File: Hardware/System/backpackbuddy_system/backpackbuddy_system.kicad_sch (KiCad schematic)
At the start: 20 parts, among them J1 PIR, J2 Ultrasonic 2, J3 Ultrasonic 1, J4 Left Vibration 1, J5 Left Vibration 2, J6 Raspberry Pi, J7 ESP8266, J8 Right Vibration 1, J9 Right Vibration 2, Q1 Q_NMOS_GSD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

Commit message: random other sch changes
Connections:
- net ESP RESET: now reaches J7.6 (Pin_6), SW1.1
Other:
- moved on the sheet: SW1
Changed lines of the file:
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@@
   (junction (at 181.61 153.67) (diameter 0) (color 0 0 0 0)
   )
-  (junction (at 217.17 63.5) (diameter 0) (color 0 0 0 0)
-  )
   (junction (at 222.25 135.89) (diameter 0) (color 0 0 0 0)
   )
@@
     (stroke (width 0) (type default) (color 0 0 0 0))
   )
+  (wire (pts (xy 232.41 62.23) (xy 243.84 62.23))
+    (stroke (width 0) (type default) (color 0 0 0 0))
+  )
   (wire (pts (xy 194.31 86.36) (xy 189.23 86.36))
     (stroke (width 0) (type default) (color 0 0 0 0))
@@
     (stroke (width 0) (type default) (color 0 0 0 0))
   )
-  (wire (pts (xy 212.09 63.5) (xy 217.17 63.5))
-    (stroke (width 0) (type default) (color 0 0 0 0))
-  )
   (wire (pts (xy 132.08 60.96) (xy 55.88 60.96))
     (stroke (width 0) (type default) (color 0 0 0 0))
@@
     (stroke (width 0) (type default) (color 0 0 0 0))
   )
-  (wire (pts (xy 217.17 38.1) (xy 217.17 63.5))
+  (wire (pts (xy 217.17 38.1) (xy 217.17 67.31))
     (stroke (width 0) (type default) (color 0 0 0 0))
   )
@@
     (stroke (width 0) (type default) (color 0 0 0 0))
   )
-  (wire (pts (xy 217.17 67.31) (xy 217.17 63.5))
-    (stroke (width 0) (type default) (color 0 0 0 0))
-  )
   (wire (pts (xy 119.38 96.52) (xy 118.11 96.52))
     (stroke (width 0) (type default) (color 0 0 0 0))
@@
     (stroke (width 0) (type default) (color 0 0 0 0))
   )
+  (wire (pts (xy 256.54 62.23) (xy 256.54 68.58))
+    (stroke (width 0) (type default) (color 0 0 0 0))
+  )
   (wire (pts (xy 102.87 118.11) (xy 132.08 118.11))
     (stroke (width 0) (type default) (color 0 0 0 0))
@@
     (stroke (width 0) (type default) (color 0 0 0 0))
   )
+  (wire (pts (xy 254 62.23) (xy 256.54 62.23))
+    (stroke (width 0) (type default) (color 0 0 0 0))
+  )
   (wire (pts (xy 163.83 120.65) (xy 163.83 123.19))
     (stroke (width 0) (type default) (color 0 0 0 0))
@@
     (stroke (width 0) (type default) (color 0 0 0 0))
   )
-  (wire (pts (xy 201.93 50.8) (xy 201.93 63.5))
-    (stroke (width 0) (type default) (color 0 0 0 0))
-  )
   (wire (pts (xy 222.25 153.67) (xy 226.06 153.67))
     (stroke (width 0) (type default) (color 0 0 0 0))
@@
     (stroke (width 0) (type default) (color 0 0 0 0))
   )
-  (wire (pts (xy 218.44 50.8) (xy 201.93 50.8))
+  (wire (pts (xy 195.58 50.8) (xy 218.44 50.8))
     (stroke (width 0) (type default) (color 0 0 0 0))
   )
@@
   (text "Debug LEDs" (at 48.26 111.76 0)
     (effects (font (size 3 3)) (justify left bottom))
+  )
+  (label "ESP RESET" (at 195.58 50.8 0)
+    (effects (font (size 1.27 1.27)) (justify left bottom))
+  )
+  (label "ESP RESET" (at 232.41 62.23 0)
+    (effects (font (size 1.27 1.27)) (justify left bottom))
   )
   (symbol (lib_id "Device:LED") (at 55.88 91.44 90) (unit 1)
@@
     (pin "1")
   )
+  (symbol (lib_id "power:GND") (at 256.54 68.58 0) (unit 1)
+    (in_bom yes) (on_board yes) (fields_autoplaced)
+    (property "Reference" "#PWR0106" (id 0) (at 256.54 74.93 0)
+      (effects (font (size 1.27 1.27)) hide)
+    )
+    (property "Value" "GND" (id 1) (at 256.54 73.66 0))
+    (property "Footprint" "" (id 2) (at 256.54 68.58 0)
+      (effects (font (size 1.27 1.27)) hide)
+    )
+    (property "Datasheet" "" (id 3) (at 256.54 68.58 0)
+      (effects (font (size 1.27 1.27)) hide)
+    )
+    (pin "1")
+  )
   (symbol (lib_id "power:GND") (at 120.65 106.68 0) (unit 1)
     (in_bom yes) (on_board yes) (fields_autoplaced)
@@
     (pin "1")
   )
-  (symbol (lib_id "Switch:SW_Push") (at 207.01 63.5 0) (unit 1)
-    (in_bom yes) (on_board yes) (fields_autoplaced)
-    (property "Reference" "SW1" (id 0) (at 207.01 55.88 0))
-    (property "Value" "ESP8266 RESET" (id 1) (at 207.01 58.42 0))
-    (property "Footprint" "BackpackBuddyFootprintLibrary:RST_SW" (id 2) (at 207.01 58.42 0)
-      (effects (font (size 1.27 1.27)) hide)
-    )
-    (property "Datasheet" "https://www.nkkswitches.com/pdf/HP03-2.pdf" (id 3) (at 207.01 58.42 0)
-      (effects (font (size 1.27 1.27)) hide)
-    )
-    (property "MPN" "HP0315AFKP2-R" (id 4) (at 207.01 63.5 0)
-      (effects (font (size 1.27 1.27)) hide)
-    )
-    (property "Stock" "https://www.digikey.com/en/products/detail/nkk-switches/HP0315AFKP2-R/1242035" (id 5) (at 207.01 63.5 0)
+  (symbol (lib_id "Switch:SW_Push") (at 248.92 62.23 0) (unit 1)
+    (in_bom yes) (on_board yes) (fields_autoplaced)
+    (property "Reference" "SW1" (id 0) (at 248.92 54.61 0))
+    (property "Value" "ESP8266 RESET" (id 1) (at 248.92 57.15 0))
+    (property "Footprint" "BackpackBuddyFootprintLibrary:RST_SW" (id 2) (at 248.92 57.15 0)
+      (effects (font (size 1.27 1.27)) hide)
+    )
+    (property "Datasheet" "https://www.nkkswitches.com/pdf/HP03-2.pdf" (id 3) (at 248.92 57.15 0)
+      (effects (font (size 1.27 1.27)) hide)
+    )
+    (property "MPN" "HP0315AFKP2-R" (id 4) (at 248.92 62.23 0)
+      (effects (font (size 1.27 1.27)) hide)
+    )
+    (property "Stock" "https://www.digikey.com/en/products/detail/nkk-switches/HP0315AFKP2-R/1242035" (id 5) (at 248.92 62.23 0)
       (effects (font (size 1.27 1.27)) hide)
     )
@@
       (reference "#PWR027") (unit 1) (value "+5V") (footprint "")
     )
-    (path "/31ba9691-809e-422e-95e0-c0a31dc5a8d2/2d2d534c-95dd-4dc9-8221-40b9e29ac241"
-      (reference "#PWR028") (unit 1) (value "+9V") (footprint "")
-    )
     (path "/31ba9691-809e-422e-95e0-c0a31dc5a8d2/3c25f8ff-3d21-4292-8719-69c0a5ba006e"
       (reference "#PWR029") (unit 1) (value "GND") (footprint "")
@@
       (reference "#PWR035") (unit 1) (value "GND") (footprint "")
     )
-    (path "/31ba9691-809e-422e-95e0-c0a31dc5a8d2/a12e409d-bf49-46f4-b410-3f940909f93b"
-      (reference "#PWR036") (unit 1) (value "+9V") (footprint "")
-    )
     (path "/31ba9691-809e-422e-95e0-c0a31dc5a8d2/b76c93d5-59d4-4a1e-aa4e-2855faa8d3bd"
       (reference "#PWR037") (unit 1) (value "+5V") (footprint "")
@@
       (reference "#PWR0105") (unit 1) (value "GND") (footprint "")
     )
+    (path "/24694138-69a7-4d98-a128-6549f6c32771"
+      (reference "#PWR0106") (unit 1) (value "GND") (footprint "")
+    )
     (path "/af61f2eb-3376-4189-8310-620a433ef8ef/f4662e9e-a042-421d-9aa3-93a911a6004a"
       (reference "C1") (unit 1) (value "10pF") (footprint "Capacitor_SMD:C_0805_2012Metric_Pad1.18x1.45mm_HandSolder")
@@
     )
     (path "/31ba9691-809e-422e-95e0-c0a31dc5a8d2/12649009-7fa5-45ae-94be-e62b9e763213"
-      (reference "J11") (unit 1) (value "Battery") (footprint "Connector_Molex:Molex_KK-254_AE-6410-03A_1x03_P2.54mm_Vertical")
+      (reference "J11") (unit 1) (value "Battery") (footprint "Connector_PinHeader_2.54mm:PinHeader_1x03_P2.54mm_Vertical")
     )
     (path "/31ba9691-809e-422e-95e0-c0a31dc5a8d2/9ea34af7-405e-4360-b874-9b4cc86b0744"
-      (reference "JP1") (unit 1) (value "SolderJumper_2_Open") (footprint "Jumper:SolderJumper-2_P1.3mm_Open_RoundedPad1.0x1.5mm")
+      (reference "JP1") (unit 1) (value "PP Short") (footprint "Jumper:SolderJumper-2_P1.3mm_Open_RoundedPad1.0x1.5mm")
     )
     (path "/31ba9691-809e-422e-95e0-c0a31dc5a8d2/25c24f9c-10e4-491d-ae1c-d8d731fa9c2b"

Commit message: fixed layout errors
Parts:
- R10, R11, R12, R13: footprint Resistor_SMD:R_0603_1608Metric_Pad1.05x0.95mm_HandSolder -> Resistor_SMD:R_0603_1608Metric_Pad0.98x0.95mm_HandSolder
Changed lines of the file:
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@@
       (effects (font (size 1.27 1.27)) (justify left))
     )
-    (property "Footprint" "Resistor_SMD:R_0603_1608Metric_Pad1.05x0.95mm_HandSolder" (id 2) (at 74.422 81.28 90)
+    (property "Footprint" "Resistor_SMD:R_0603_1608Metric_Pad0.98x0.95mm_HandSolder" (id 2) (at 74.422 81.28 90)
       (effects (font (size 1.27 1.27)) hide)
     )
@@
       (effects (font (size 1.27 1.27)) (justify left))
     )
-    (property "Footprint" "Resistor_SMD:R_0603_1608Metric_Pad1.05x0.95mm_HandSolder" (id 2) (at 64.262 81.28 90)
+    (property "Footprint" "Resistor_SMD:R_0603_1608Metric_Pad0.98x0.95mm_HandSolder" (id 2) (at 64.262 81.28 90)
       (effects (font (size 1.27 1.27)) hide)
     )
@@
       (effects (font (size 1.27 1.27)) (justify left))
     )
-    (property "Footprint" "Resistor_SMD:R_0603_1608Metric_Pad1.05x0.95mm_HandSolder" (id 2) (at 42.672 81.28 90)
+    (property "Footprint" "Resistor_SMD:R_0603_1608Metric_Pad0.98x0.95mm_HandSolder" (id 2) (at 42.672 81.28 90)
       (effects (font (size 1.27 1.27)) hide)
     )
@@
       (effects (font (size 1.27 1.27)) (justify left))
     )
-    (property "Footprint" "Resistor_SMD:R_0603_1608Metric_Pad1.05x0.95mm_HandSolder" (id 2) (at 54.102 81.28 90)
+    (property "Footprint" "Resistor_SMD:R_0603_1608Metric_Pad0.98x0.95mm_HandSolder" (id 2) (at 54.102 81.28 90)
       (effects (font (size 1.27 1.27)) hide)
     )
@@
     )
     (path "/31ba9691-809e-422e-95e0-c0a31dc5a8d2/d575defe-5c9a-4b80-879c-945013e136dc"
-      (reference "C10") (unit 1) (value "1200pF") (footprint "Capacitor_SMD:C_0603_1608Metric_Pad1.05x0.95mm_HandSolder")
+      (reference "C10") (unit 1) (value "1200pF") (footprint "Capacitor_SMD:C_0603_1608Metric_Pad1.08x0.95mm_HandSolder")
     )
     (path "/31ba9691-809e-422e-95e0-c0a31dc5a8d2/fcf4fbe9-7df1-4ba3-ae92-56b4df5c8fbd"
-      (reference "C11") (unit 1) (value "0.1uF") (footprint "Capacitor_SMD:C_0603_1608Metric_Pad1.05x0.95mm_HandSolder")
+      (reference "C11") (unit 1) (value "0.1uF") (footprint "Capacitor_SMD:C_0603_1608Metric_Pad1.08x0.95mm_HandSolder")
     )
     (path "/31ba9691-809e-422e-95e0-c0a31dc5a8d2/966b4f21-a7ae-46d1-ac5e-1acb6c4d484d"
-      (reference "C12") (unit 1) (value "0.22uF") (footprint "Capacitor_SMD:C_0603_1608Metric_Pad1.05x0.95mm_HandSolder")
+      (reference "C12") (unit 1) (value "0.22uF") (footprint "Capacitor_SMD:C_0603_1608Metric_Pad1.08x0.95mm_HandSolder")
     )
     (path "/31ba9691-809e-422e-95e0-c0a31dc5a8d2/f2de3336-c569-4c02-a0ec-1c644f8fd673"
@@
     )
     (path "/31ba9691-809e-422e-95e0-c0a31dc5a8d2/0713b6db-e506-43b9-814c-91d8edab0f04"
-      (reference "C14") (unit 1) (value "0.47uF") (footprint "Capacitor_SMD:C_0603_1608Metric_Pad1.05x0.95mm_HandSolder")
+      (reference "C14") (unit 1) (value "0.47uF") (footprint "Capacitor_SMD:C_0603_1608Metric_Pad1.08x0.95mm_HandSolder")
     )
     (path "/31ba9691-809e-422e-95e0-c0a31dc5a8d2/9ac44638-509c-4c3e-b7d7-b47ebab9679e"
@@
     )
     (path "/31ba9691-809e-422e-95e0-c0a31dc5a8d2/d52e8af1-7540-499e-b62d-baa8cf06903a"
-      (reference "R4") (unit 1) (value "39k") (footprint "Resistor_SMD:R_0603_1608Metric_Pad1.05x0.95mm_HandSolder")
+      (reference "R4") (unit 1) (value "39k") (footprint "Resistor_SMD:R_0603_1608Metric_Pad0.98x0.95mm_HandSolder")
     )
     (path "/31ba9691-809e-422e-95e0-c0a31dc5a8d2/0832bfd1-c319-4bdf-ae46-55bc81b56fa4"
-      (reference "R5") (unit 1) (value "1k") (footprint "Resistor_SMD:R_0603_1608Metric_Pad1.05x0.95mm_HandSolder")
+      (reference "R5") (unit 1) (value "1k") (footprint "Resistor_SMD:R_0603_1608Metric_Pad0.98x0.95mm_HandSolder")
     )
     (path "/31ba9691-809e-422e-95e0-c0a31dc5a8d2/98487a5e-4abe-4989-9b3e-a834c5004a17"
-      (reference "R6") (unit 1) (value "1k") (footprint "Resistor_SMD:R_0603_1608Metric_Pad1.05x0.95mm_HandSolder")
+      (reference "R6") (unit 1) (value "1k") (footprint "Resistor_SMD:R_0603_1608Metric_Pad0.98x0.95mm_HandSolder")
     )
     (path "/31ba9691-809e-422e-95e0-c0a31dc5a8d2/4f13f290-5197-4913-a65d-06ac02a6a329"
-      (reference "R7") (unit 1) (value "1k") (footprint "Resistor_SMD:R_0603_1608Metric_Pad1.05x0.95mm_HandSolder")
+      (reference "R7") (unit 1) (value "1k") (footprint "Resistor_SMD:R_0603_1608Metric_Pad0.98x0.95mm_HandSolder")
     )
     (path "/31ba9691-809e-422e-95e0-c0a31dc5a8d2/8e70fbf7-3f87-4745-a46c-c8c947fb7862"
-      (reference "R8") (unit 1) (value "1k") (footprint "Resistor_SMD:R_0603_1608Metric_Pad1.05x0.95mm_HandSolder")
+      (reference "R8") (unit 1) (value "1k") (footprint "Resistor_SMD:R_0603_1608Metric_Pad0.98x0.95mm_HandSolder")
     )
     (path "/31ba9691-809e-422e-95e0-c0a31dc5a8d2/6e8a8847-bd59-48a8-8db0-43b63737c316"
-      (reference "R9") (unit 1) (value "1k") (footprint "Resistor_SMD:R_0603_1608Metric_Pad1.05x0.95mm_HandSolder")
+      (reference "R9") (unit 1) (value "1k") (footprint "Resistor_SMD:R_0603_1608Metric_Pad0.98x0.95mm_HandSolder")
     )
     (path "/89d8bea6-34ba-421f-b668-e88c2471b447"
-      (reference "R10") (unit 1) (value "1k") (footprint "Resistor_SMD:R_0603_1608Metric_Pad1.05x0.95mm_HandSolder")
+      (reference "R10") (unit 1) (value "1k") (footprint "Resistor_SMD:R_0603_1608Metric_Pad0.98x0.95mm_HandSolder")
     )
     (path "/d084b666-fe1b-4475-91b8-494092fcb3aa"
-      (reference "R11") (unit 1) (value "1k") (footprint "Resistor_SMD:R_0603_1608Metric_Pad1.05x0.95mm_HandSolder")
+      (reference "R11") (unit 1) (value "1k") (footprint "Resistor_SMD:R_0603_1608Metric_Pad0.98x0.95mm_HandSolder")
     )
     (path "/67a8f1e6-1068-4a7c-8d94-ef517d1cd419"
-      (reference "R12") (unit 1) (value "1k") (footprint "Resistor_SMD:R_0603_1608Metric_Pad1.05x0.95mm_HandSolder")
+      (reference "R12") (unit 1) (value "1k") (footprint "Resistor_SMD:R_0603_1608Metric_Pad0.98x0.95mm_HandSolder")
     )
     (path "/4199edad-50b0-4d93-b8bd-a6bbe5aaaa7e"
-      (reference "R13") (unit 1) (value "1k") (footprint "Resistor_SMD:R_0603_1608Metric_Pad1.05x0.95mm_HandSolder")
+      (reference "R13") (unit 1) (value "1k") (footprint "Resistor_SMD:R_0603_1608Metric_Pad0.98x0.95mm_HandSolder")
     )
     (path "/3d33362d-175b-4c68-9050-00314cb841c5"

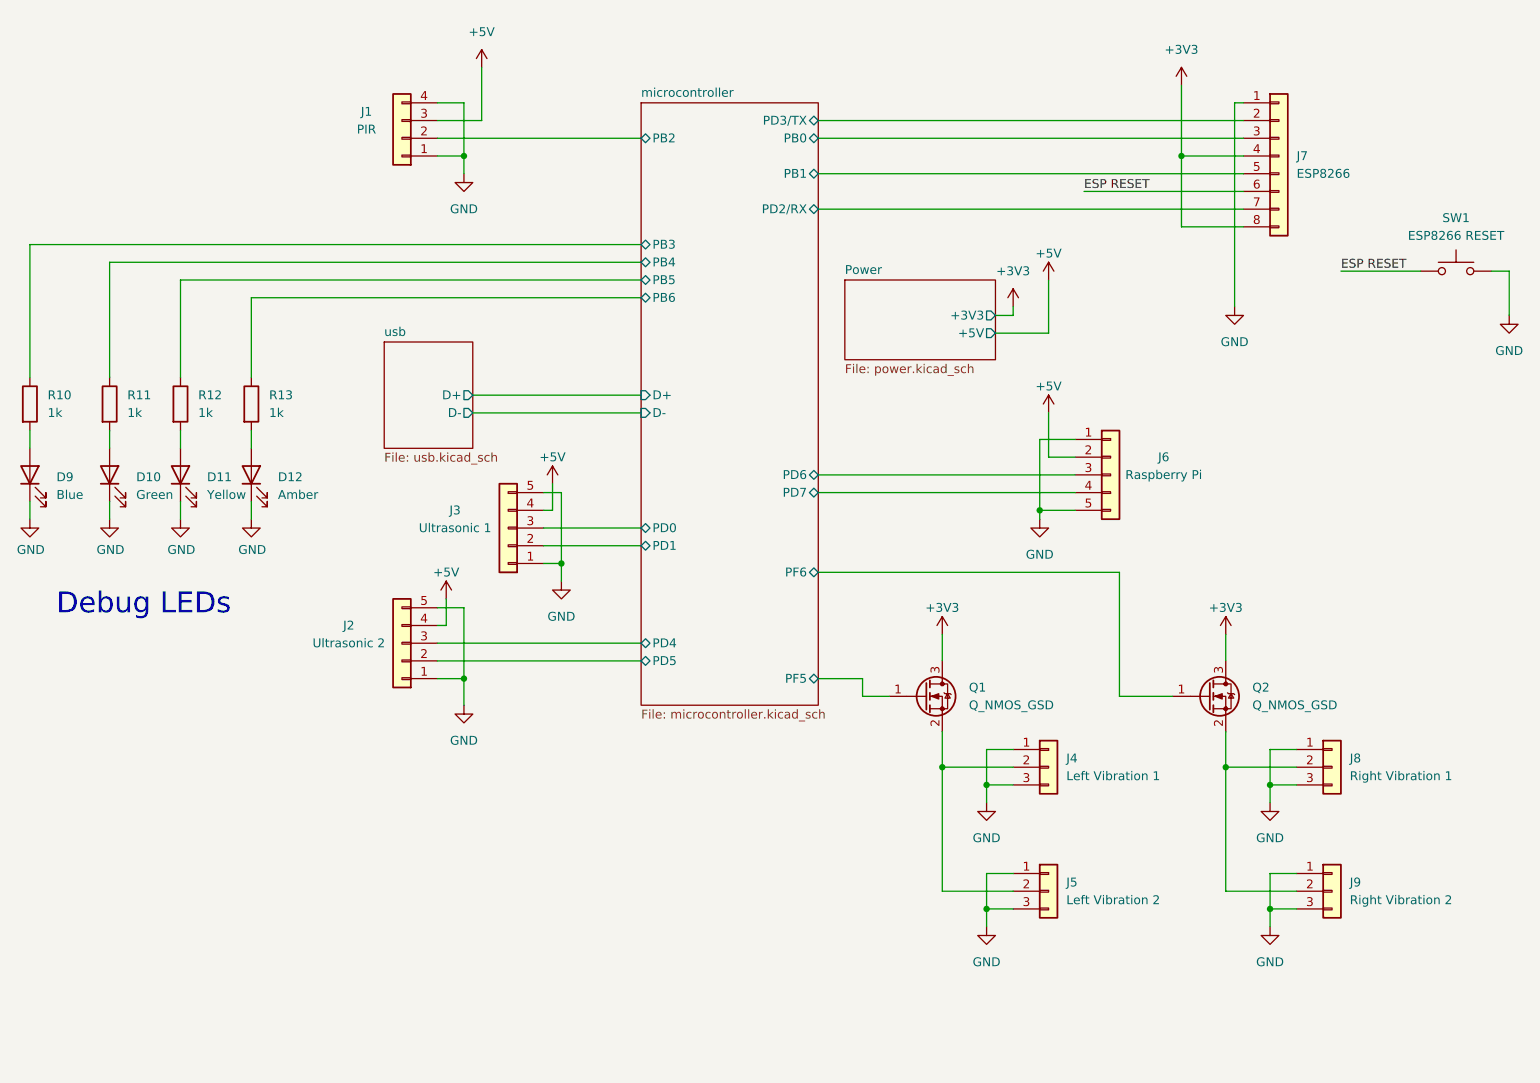
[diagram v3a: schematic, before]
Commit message: added ESP8266 footprint, more testpoints, mounting holes
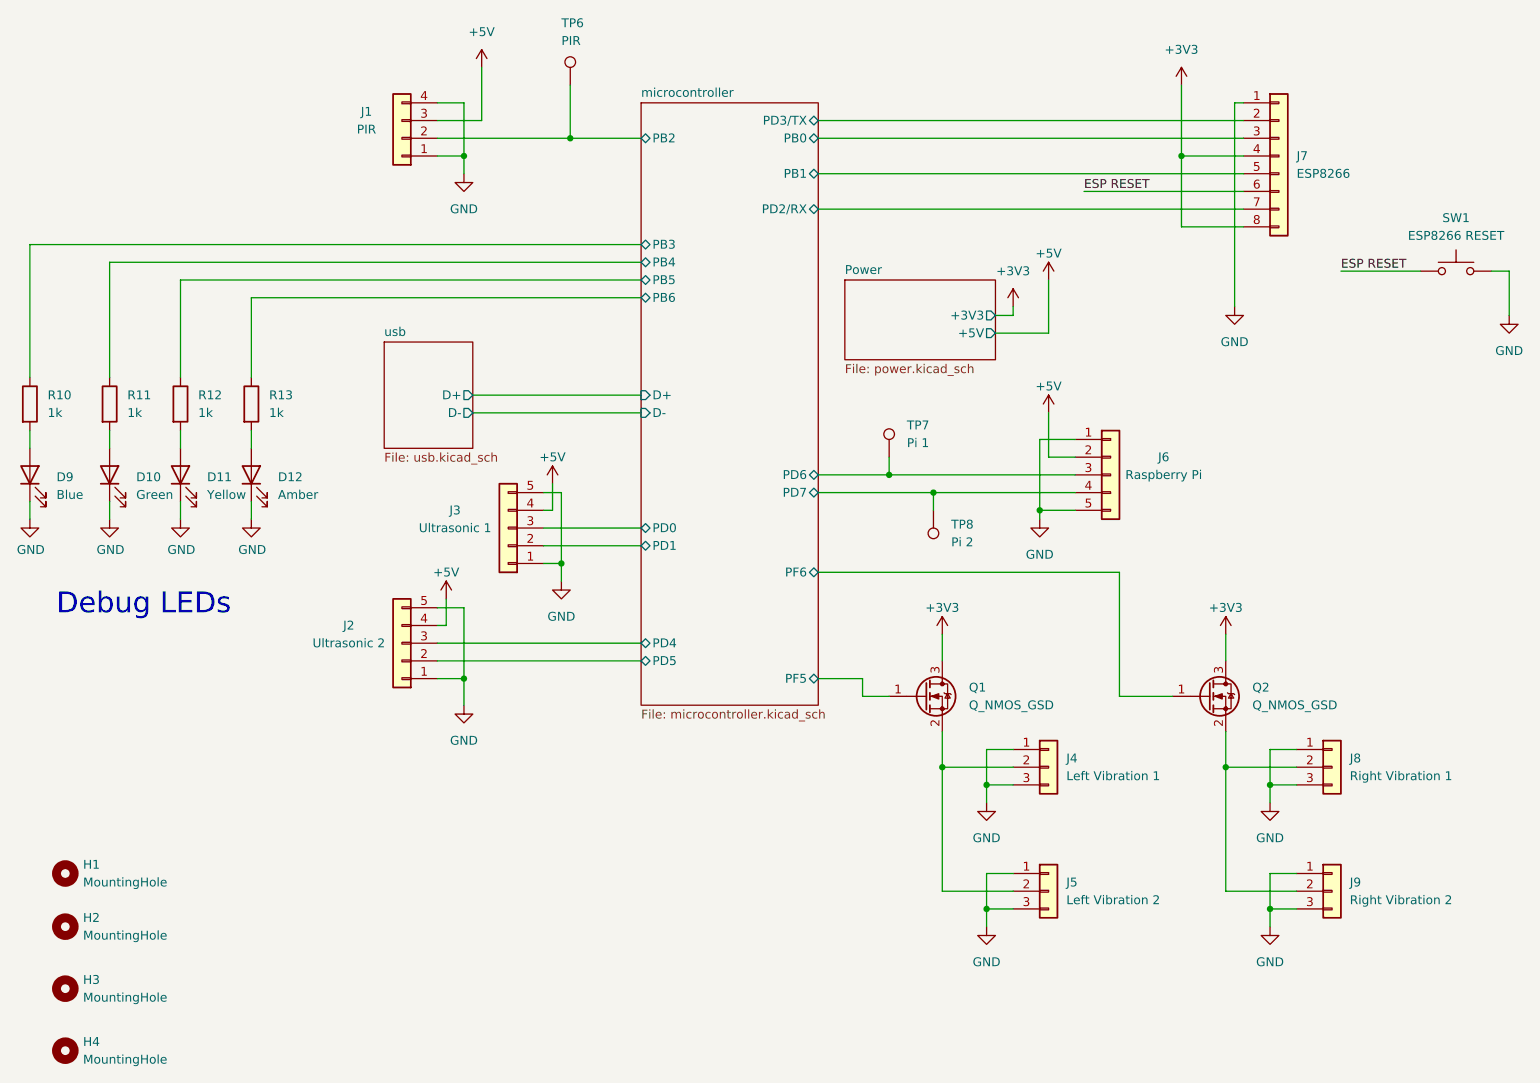
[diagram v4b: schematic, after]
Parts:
- added H1, H2, H3, H4: MountingHole, MountingHole:MountingHole_2.7mm_M2.5, symbol Mechanical:MountingHole
- added TP6: PIR, TestPoint:TestPoint_THTPad_D1.0mm_Drill0.5mm, symbol Connector:TestPoint
- added TP7: Pi 1, TestPoint:TestPoint_THTPad_D1.0mm_Drill0.5mm, symbol Connector:TestPoint
- added TP8: Pi 2, TestPoint:TestPoint_THTPad_D1.0mm_Drill0.5mm, symbol Connector:TestPoint
- J7: footprint Connector_PinHeader_2.54mm:PinHeader_2x04_P2.54mm_Vertical -> BackpackBuddyFootprintLibrary:ESP8266
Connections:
- net microcontroller/PB2: now also TP6.1
- net microcontroller/PD6: now also TP7.1
- net microcontroller/PD7: now also TP8.1
